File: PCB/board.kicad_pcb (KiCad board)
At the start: 2 copper layers, 161 parts, among them J1 Micro_SD_Card, J10 Conn_01x10, J11 Conn_01x02, J12 Conn_02x04_Odd_Even, J13 Conn_01x02, J14 Conn_01x02, J15 Conn_01x03, J16 Conn_01x02, J17 Conn_01x05, J18 Conn_01x04, J19 Conn_01x04, J2 Conn_ARM_JTAG_SWD_10, J20 Conn_01x02, J21 Conn_01x03, J22 Conn_02x04_Odd_Even, J23 Conn_01x04, J24 Conn_01x04, J25 Conn_01x02, J26 Conn_01x03, J27 Conn_02x04_Odd_Even, J28 Conn_01x04, J29 Conn_01x04, J3 USB_C_Receptacle_USB2.0_14P, J30 Conn_01x02, J31 Conn_01x03, J32 Conn_01x02, J33 Conn_01x02, J34 Conn_01x02, J35 Conn_01x02, J36 Conn_01x02, J37 Conn_01x02, J4 Conn_01x04, J5 Conn_01x04, J6 Conn_01x02, J7 Conn_01x03, J8 Conn_02x04_Odd_Even, J9 Conn_01x10, Q1 IRLML6402, Q2 NMOS, Q3 NMOS, Q4 NMOS, Q5 NMOS, Q6 NMOS, SW1 SW_Push, SW2 SW_Push, U1 STM32H743VITx, U2 AP7361C, U4 TMC Stepstick, U5 TMC Stepstick, U6 TMC Stepstick, U7 TMC Stepstick, U8 AP63203WU, Y2 25 MHz

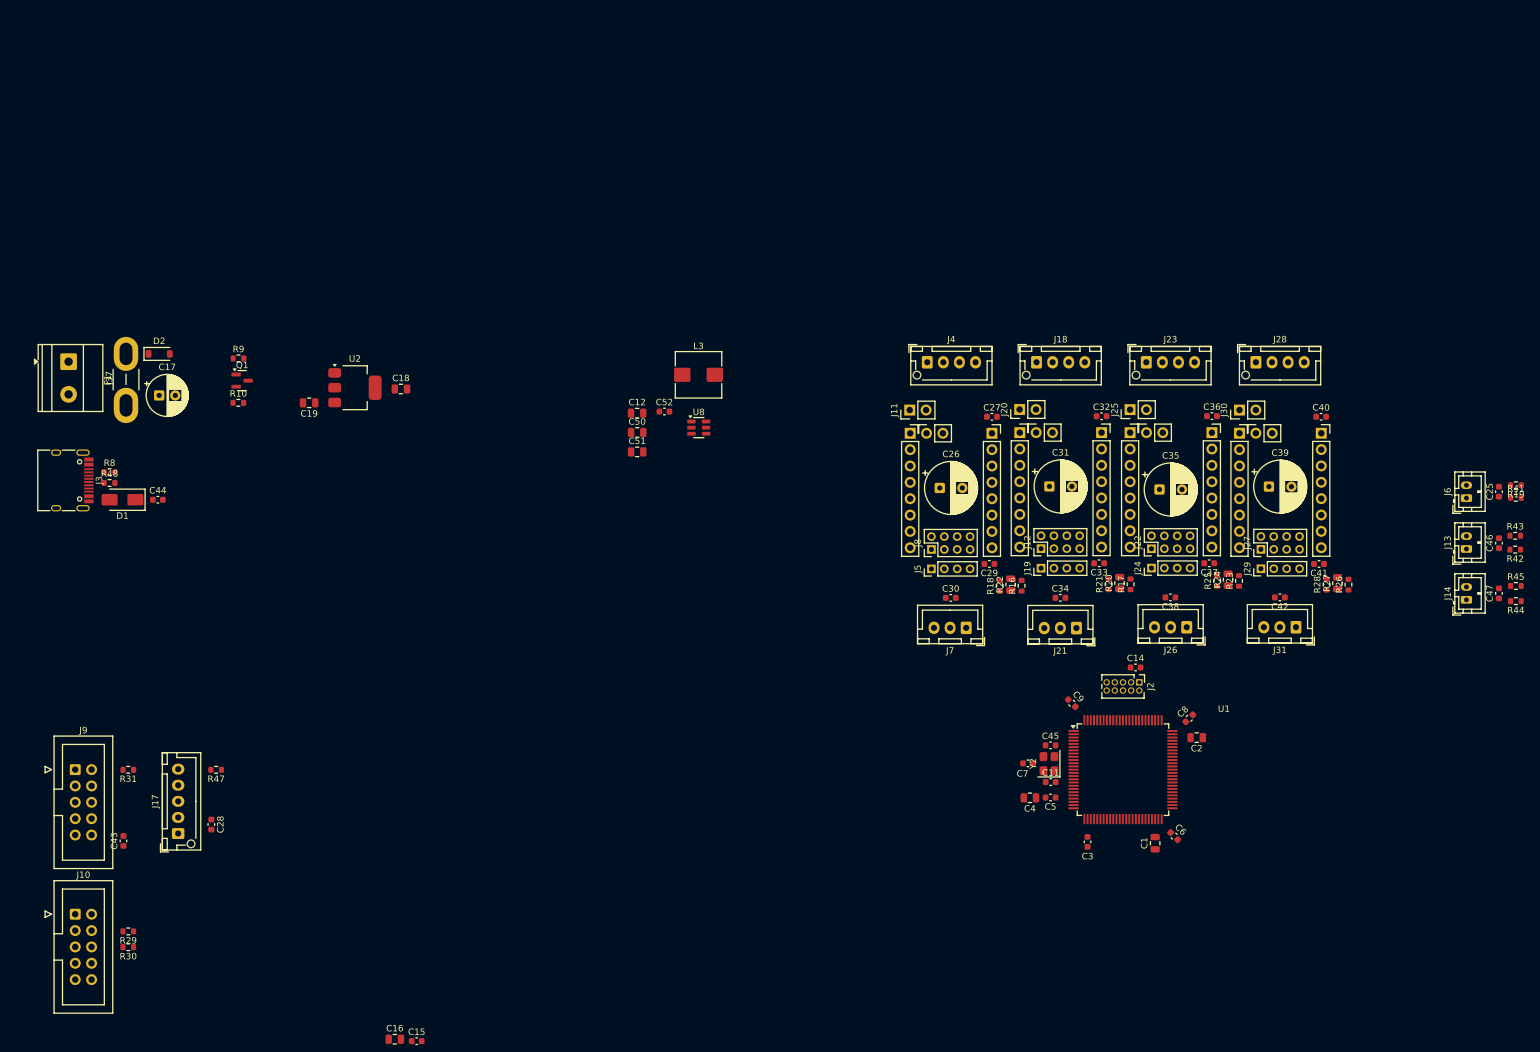
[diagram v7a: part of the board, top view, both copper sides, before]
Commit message: organizing everything into a more coherent board
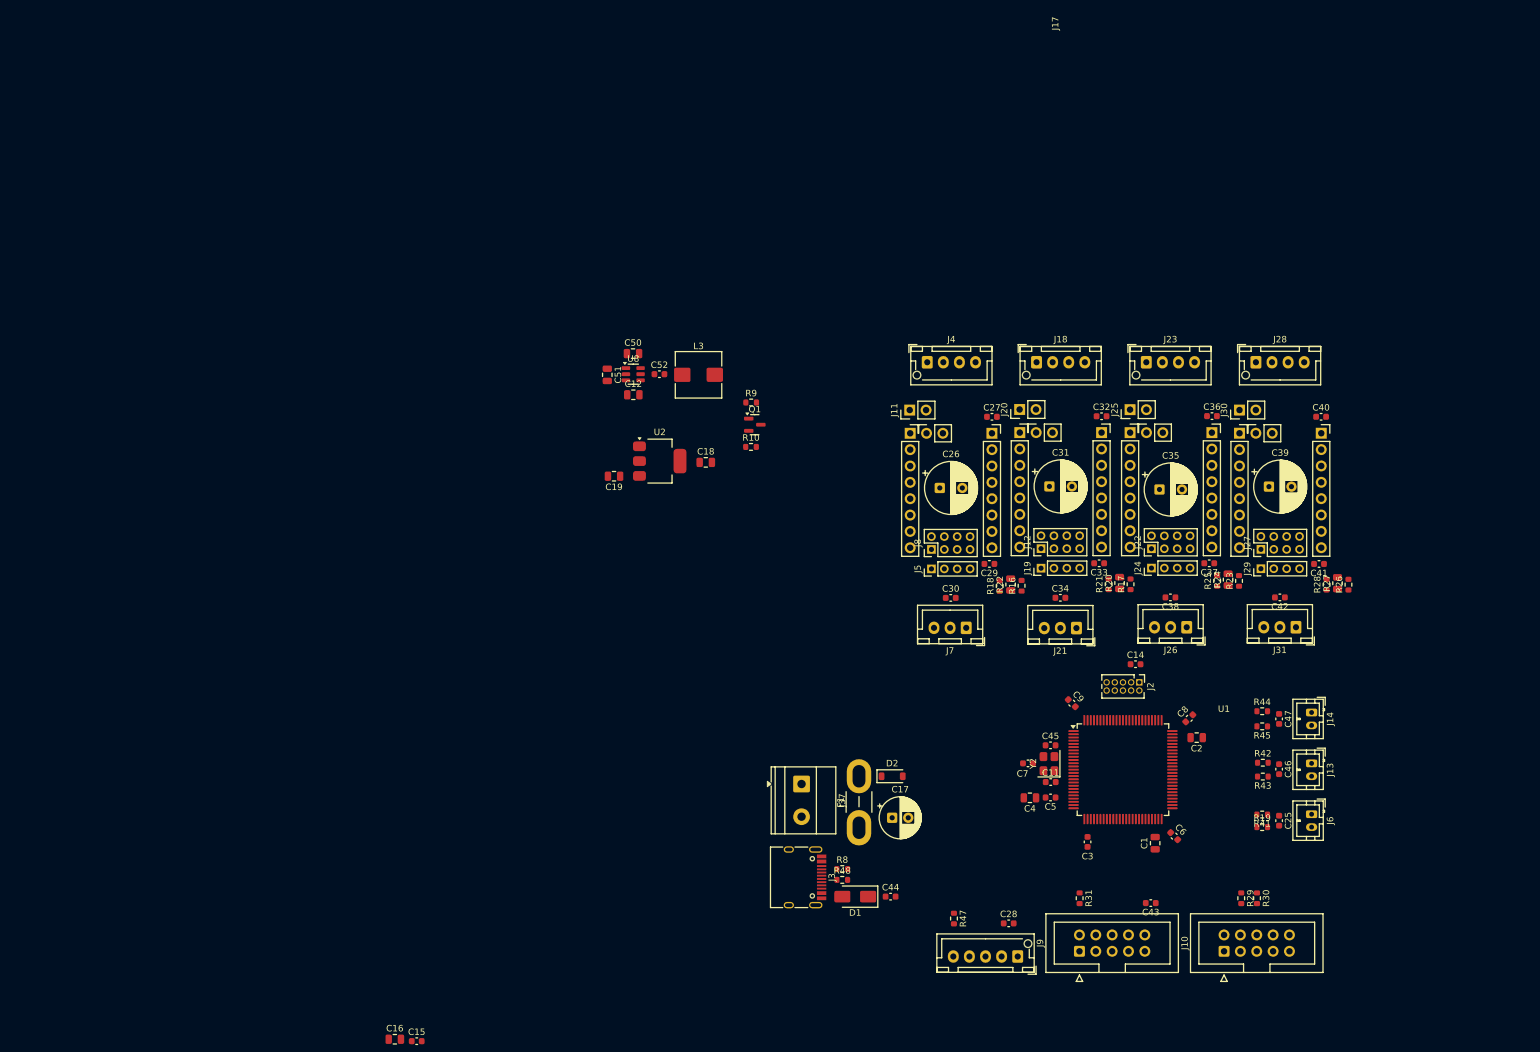
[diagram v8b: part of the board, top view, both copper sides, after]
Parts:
- moved J10 178.5 mm to (206.8, 120.1), turned to 90 degrees
- moved R30 175.5 mm to (211.9, 111.9), turned to -90 degrees
- moved R29 172.9 mm to (209.5, 111.9), turned to -90 degrees
- moved C43 159.9 mm to (195.4, 112.7), turned to 180 degrees
- moved J9 158.5 mm to (184.3, 120.1), turned to 90 degrees
- moved R31 149.1 mm to (184.4, 111.9), turned to -90 degrees
- moved J17 131.8 mm to (174.8, 121.0), turned to 180 degrees
- moved C17 131.4 mm to (155.2, 99.4)
- moved D2 131.4 mm to (155.2, 93.0)
- moved F1 131.4 mm to (150.1, 101.0)
- moved J37 131.4 mm to (141.2, 94.2)
- moved J3 129.4 mm to (140.2, 108.7)
- moved R48 129.4 mm to (147.5, 109.0)
- moved R8 129.4 mm to (147.5, 107.4)
- moved C44 129.4 mm to (155.0, 111.7)
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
